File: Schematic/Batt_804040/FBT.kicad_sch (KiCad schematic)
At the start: 20 parts, among them J1 TRRS Connector 3.5, J2 TRRS Connector 3.5, SW1 SW_SPDT, U1 HT7333-1-TO92

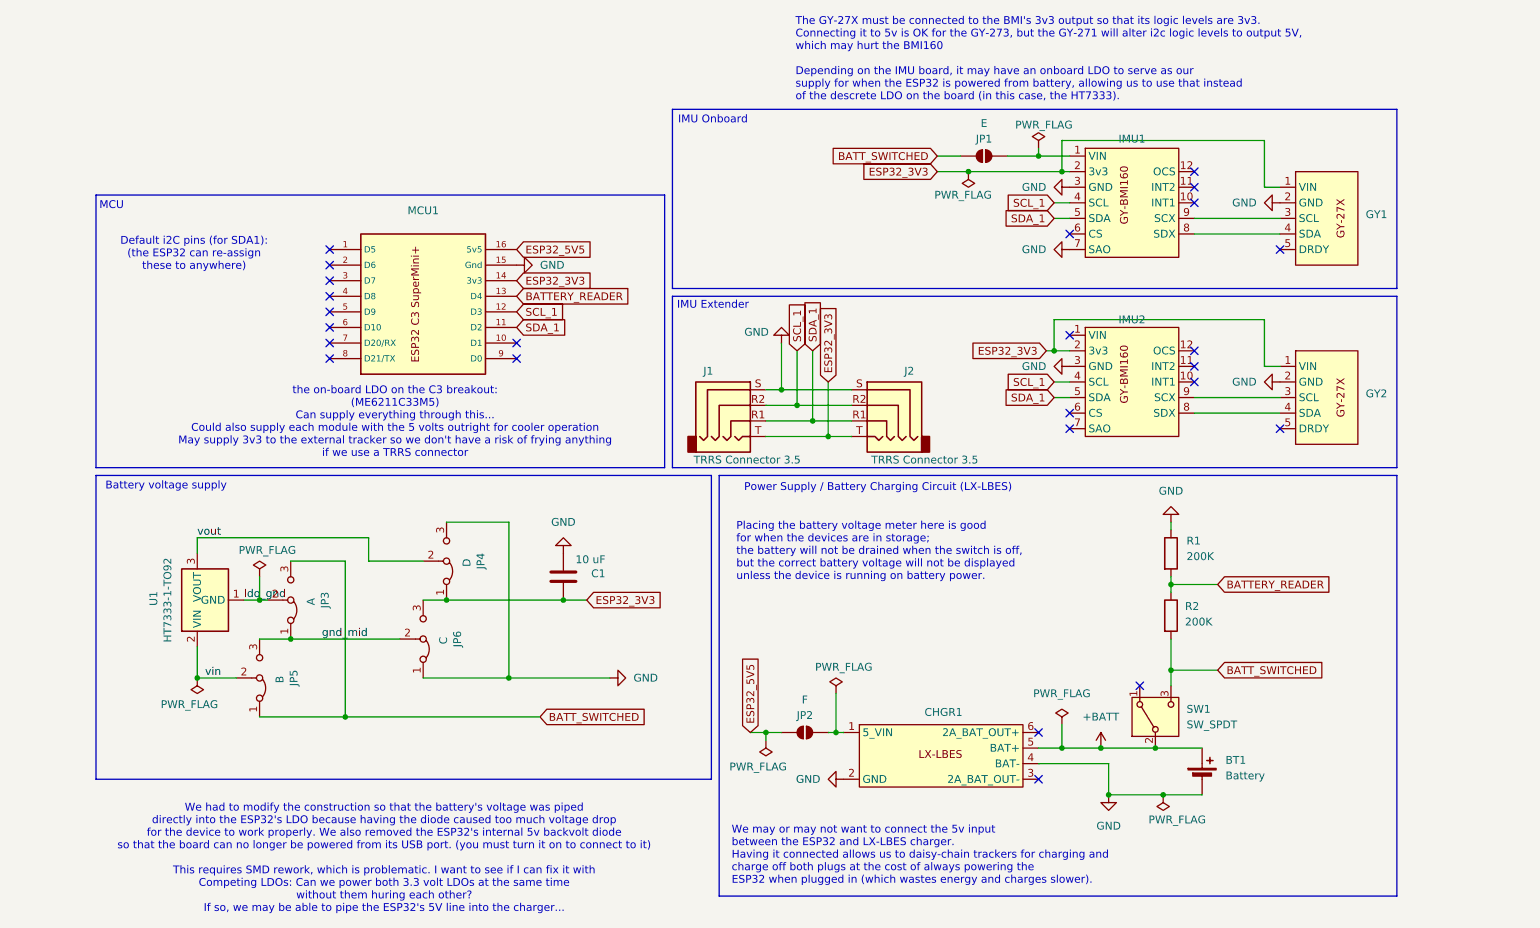
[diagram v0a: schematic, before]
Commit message: Work on documentation, fix Mr. Tracker Jumpers
The Rev 3.0 PCB unfortunately can't accommodate all regulator configs due to a mistake in the pin layout (forgetting which pins went where in the schematic)

This was resolved for Mr. Tracker
TODO: Mrs. Tracker
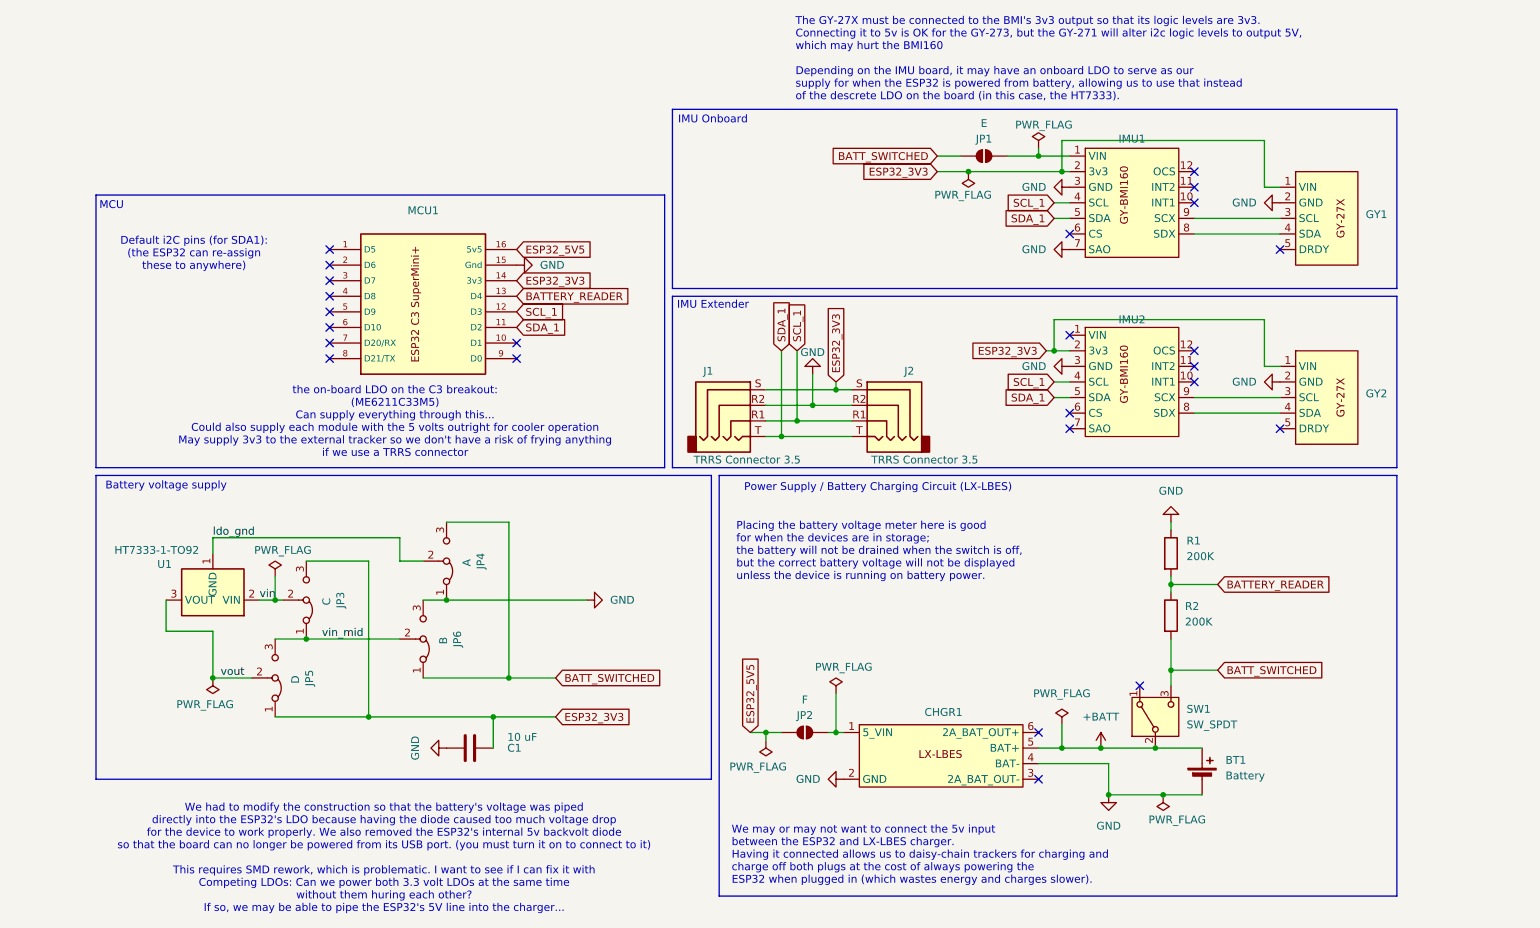
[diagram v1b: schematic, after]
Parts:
- JP3: value A -> C
- JP4: value D -> A
- JP5: value B -> D
- JP6: value C -> B
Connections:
- net BATT_SWITCHED: now also JP4.3 (B), JP6.1 (A); no longer JP3.3 (B), JP5.1 (A)
- net ESP32_3V3: now also J1.S, J2.S, JP3.3 (B), JP5.1 (A); no longer J1.T, J2.T, JP4.1 (A), JP6.3 (B)
- net GND: now also J1.R2, J2.R2, JP4.1 (A), JP6.3 (B); no longer J1.S, J2.S, JP4.3 (B), JP6.1 (A)
- net SCL_1: now also J1.R1, J2.R1; no longer J1.R2, J2.R2
- net SDA_1: now also J1.T, J2.T; no longer J1.R1, J2.R1
- net ldo_gnd: now also JP4.2 (C); no longer JP3.2 (C)
- net vin: now also JP3.2 (C); no longer JP5.2 (C)
- net vout: now also JP5.2 (C); no longer JP4.2 (C)
- net gnd_mid renamed vin_mid
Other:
- moved on the sheet: C1, JP3, JP5, U1
